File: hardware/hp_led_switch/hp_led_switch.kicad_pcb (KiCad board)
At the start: 2 copper layers, 45.5 x 71 mm, 30 parts, among them J1 Conn_01x04, J2 Conn_01x04, J3 Conn_01x02, J4 Conn_01x02, J5 Conn_01x02, J6 Conn_01x02, J7 Conn_01x02, J8 Conn_01x02, Q1 IRLZ44N, Q2 IRLZ44N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

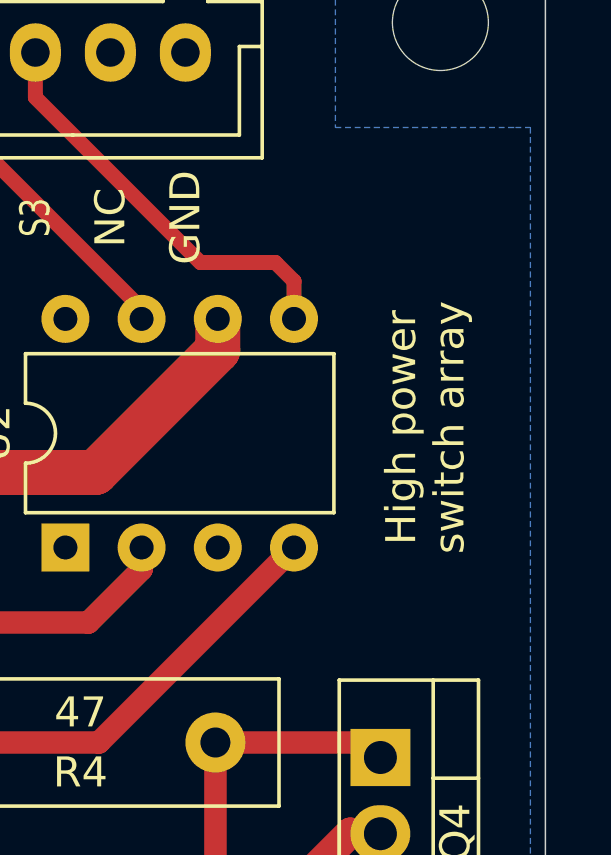
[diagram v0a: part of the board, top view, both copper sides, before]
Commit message: Add version number to boards
Add version number to boards and update screenshots, zip gerber archives
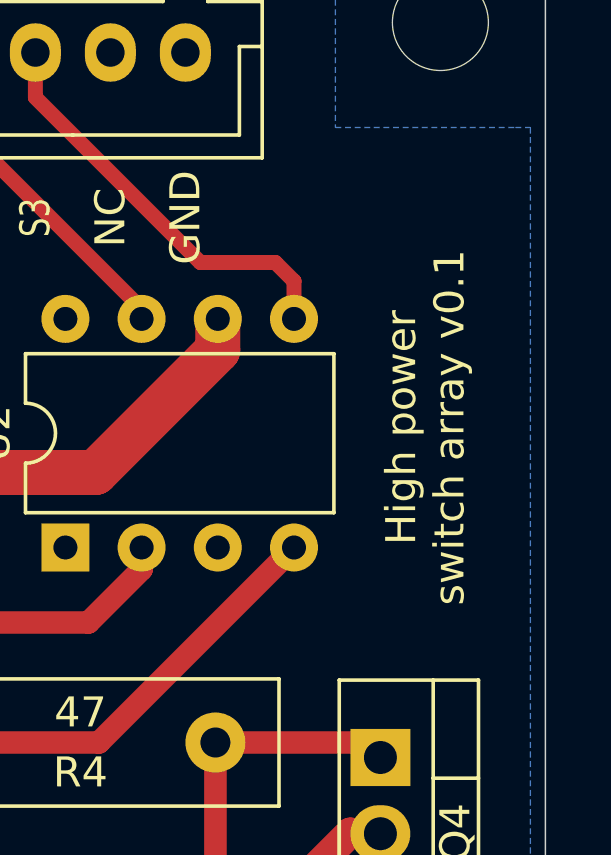
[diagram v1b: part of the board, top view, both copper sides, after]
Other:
- board text added: "High power switch array v0.1"
- board text removed: "High power switch array"

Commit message: Apply CERN-W license
Apply CERN-W license to all boards, move the first iteration of the IR_sensor to the archive

Co-Authored-By: Andre Maia Chagas <a.maia-chagas@sussex.ac.uk>
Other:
- board text added: "board by Ihor Sobianin licensed under CERN-OHL-W 2.0 https://ohwr.org/project/cernohl"

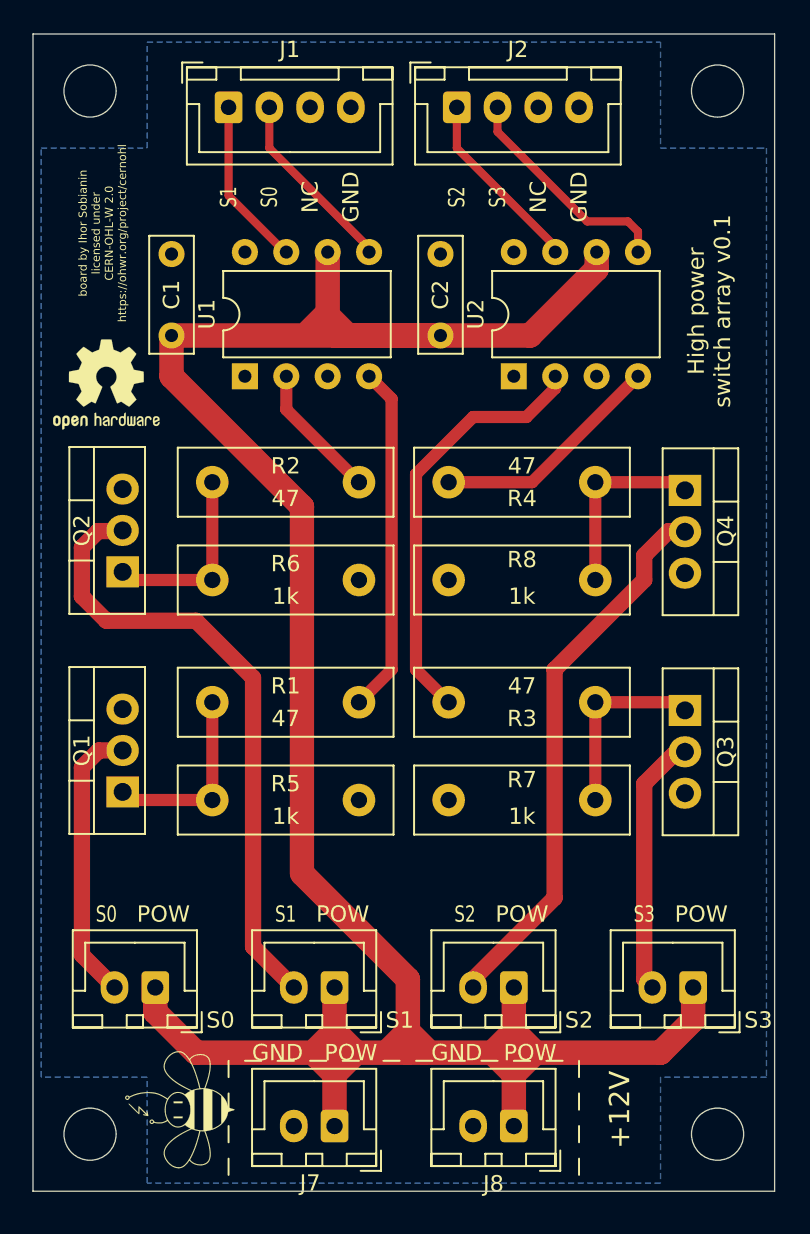
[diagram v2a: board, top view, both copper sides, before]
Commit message: Update HP switch
Update wrong tracing and connections on HP switch
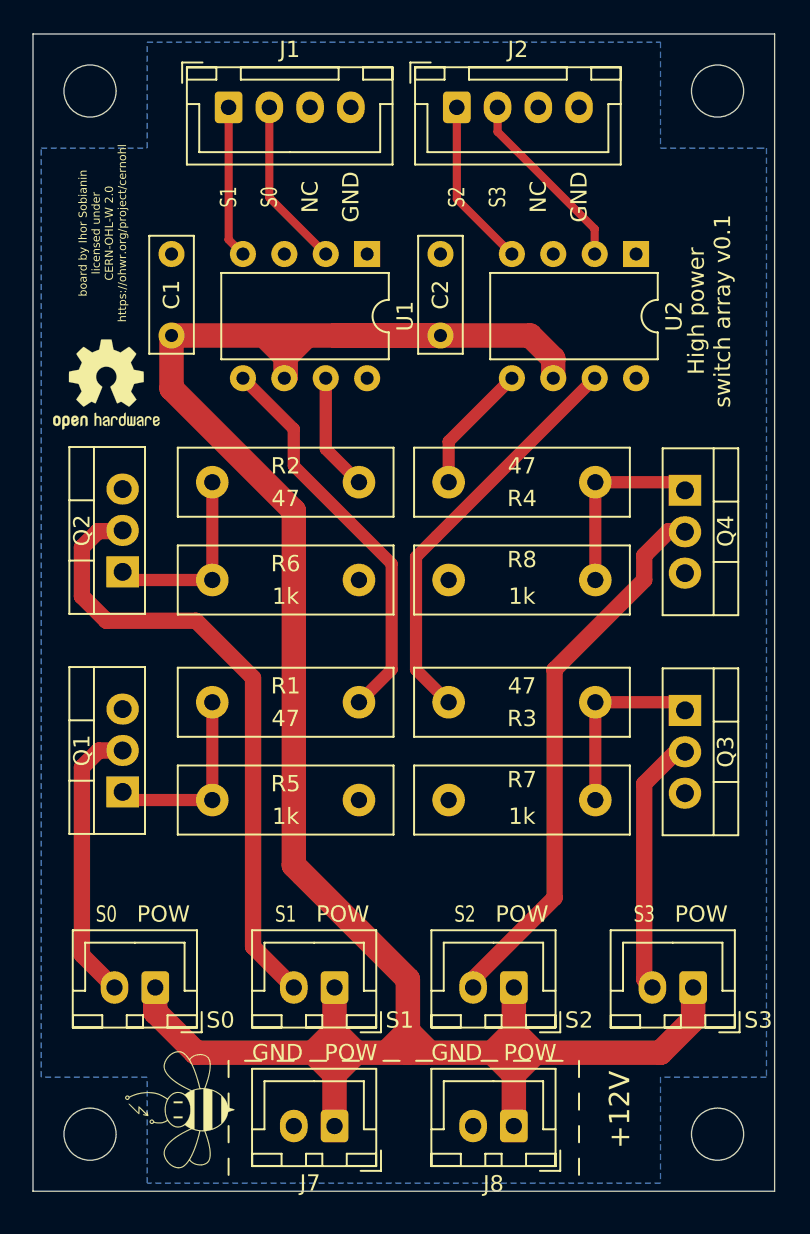
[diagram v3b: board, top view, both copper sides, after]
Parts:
- moved U1 10.6 mm to (144.5, 47.0), turned to 270 degrees
- moved U2 10.6 mm to (161.0, 47.0), turned to 270 degrees
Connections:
- J1 pad 1: OUT_0 -> IN_1
- J1 pad 2: OUT_1 -> IN_0
- J2 pad 1: OUT_2 -> IN_3
- J2 pad 2: OUT_3 -> IN_2
- U1 pad 1: GND -> (no net)
- U1 pad 2: Net-(R2-Pad1) -> OUT_0
- U1 pad 4: Net-(R1-Pad1) -> OUT_1
- U1 pad 5: OUT_1 -> Net-(R1-Pad1)
- U1 pad 7: OUT_0 -> Net-(R2-Pad1)
- U1 pad 8: GND -> (no net)
- U2 pad 1: GND -> (no net)
- U2 pad 2: Net-(R3-Pad1) -> OUT_2
- U2 pad 4: Net-(R4-Pad1) -> OUT_3
- U2 pad 5: OUT_3 -> Net-(R4-Pad1)
- U2 pad 7: OUT_2 -> Net-(R3-Pad1)
- U2 pad 8: GND -> (no net)
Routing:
- net +12V: track 171.3 -> 164.8 mm
- net Net-(R4-Pad1): track 14.3 -> 7.99 mm
- net OUT_3: track 13.9 -> 10.4 mm
- net Net-(R1-Pad1): track 21.4 -> 24.5 mm
- net OUT_1: track 11.4 -> 9.36 mm
- net Net-(R2-Pad1): track 8.35 -> 7.22 mm
- net Net-(R3-Pad1): track 26.3 -> 25.2 mm

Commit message: boards review
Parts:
- U1, U2: footprint Package_DIP:DIP-8_W7.62mm -> Package_DIP:DIP-8_W7.62mm_LongPads
- moved U1 0.17 mm to (144.4, 46.9)
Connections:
- U1 pad 2: OUT_0 -> IN_0
- U1 pad 4: OUT_1 -> IN_1
- U2 pad 2: OUT_2 -> IN_2
- U2 pad 4: OUT_3 -> IN_3
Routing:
- net IN_2: track 0.00 -> 12.5 mm
- net OUT_2: track 11.5 -> 0.00 mm
- net OUT_0: track 10.4 -> 0.00 mm
- net IN_0: track 0.00 -> 10.4 mm
- net OUT_3: track 10.4 -> 0.00 mm
- net IN_3: track 0.00 -> 10.4 mm
- net OUT_1: track 9.36 -> 0.00 mm
- net IN_1: track 0.00 -> 9.36 mm
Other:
- board text added: "High power switch array v0.2"
- board text removed: "High power switch array v0.1"
